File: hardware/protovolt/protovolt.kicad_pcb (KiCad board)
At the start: 2 copper layers, 76 parts, among them J1 Conn_01x03, J10 Conn_02x03_Odd_Even, J2 Conn_01x03, J3 Conn_01x03, J4 Conn_01x03, J5 Conn_01x03, J6 Conn_01x03, J7 Conn_01x03, J8 Conn_01x03, J9 Conn_02x03_Odd_Even, Q1 BSC0702LS, Q2 BSC0702LS, Q3 BSC0702LS, Q4 BSC0702LS, Q5 BSC0702LS, U1 INA226, U2 LM51772RHAR

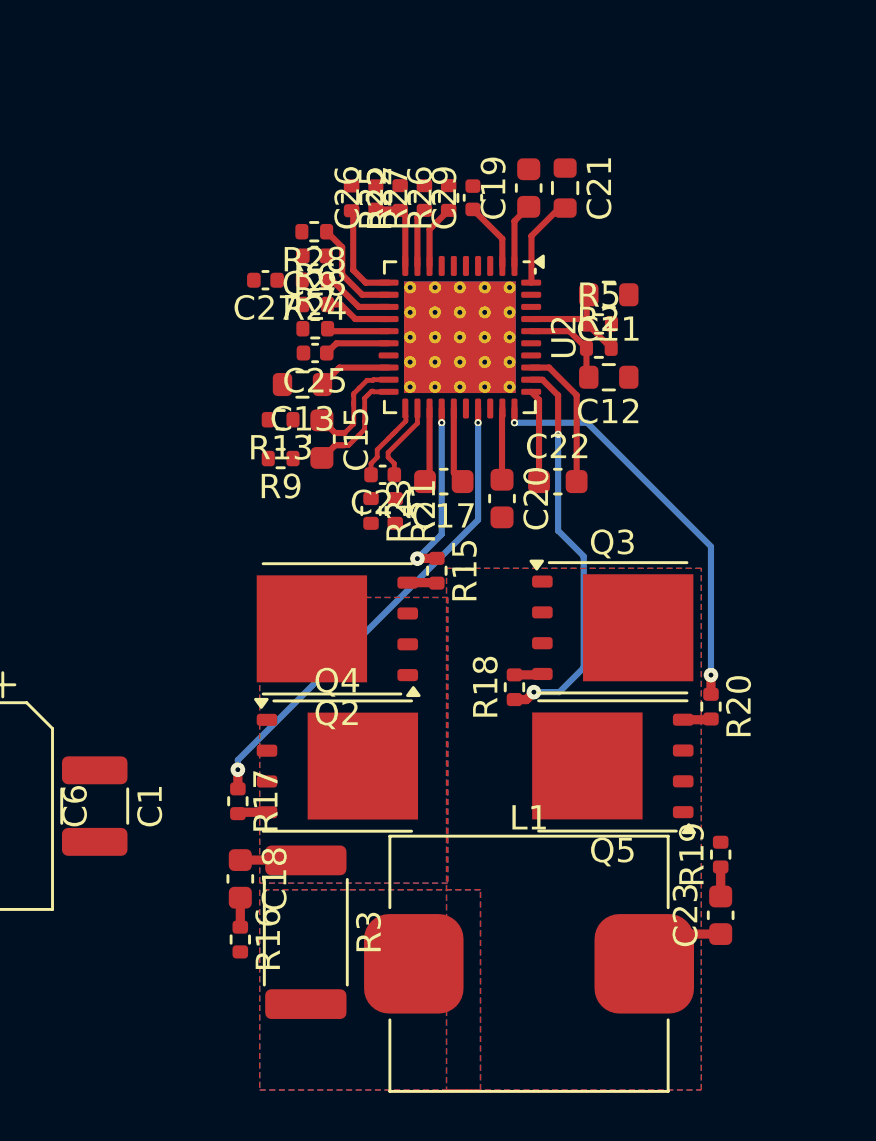
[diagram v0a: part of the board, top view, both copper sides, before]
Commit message: fet routing
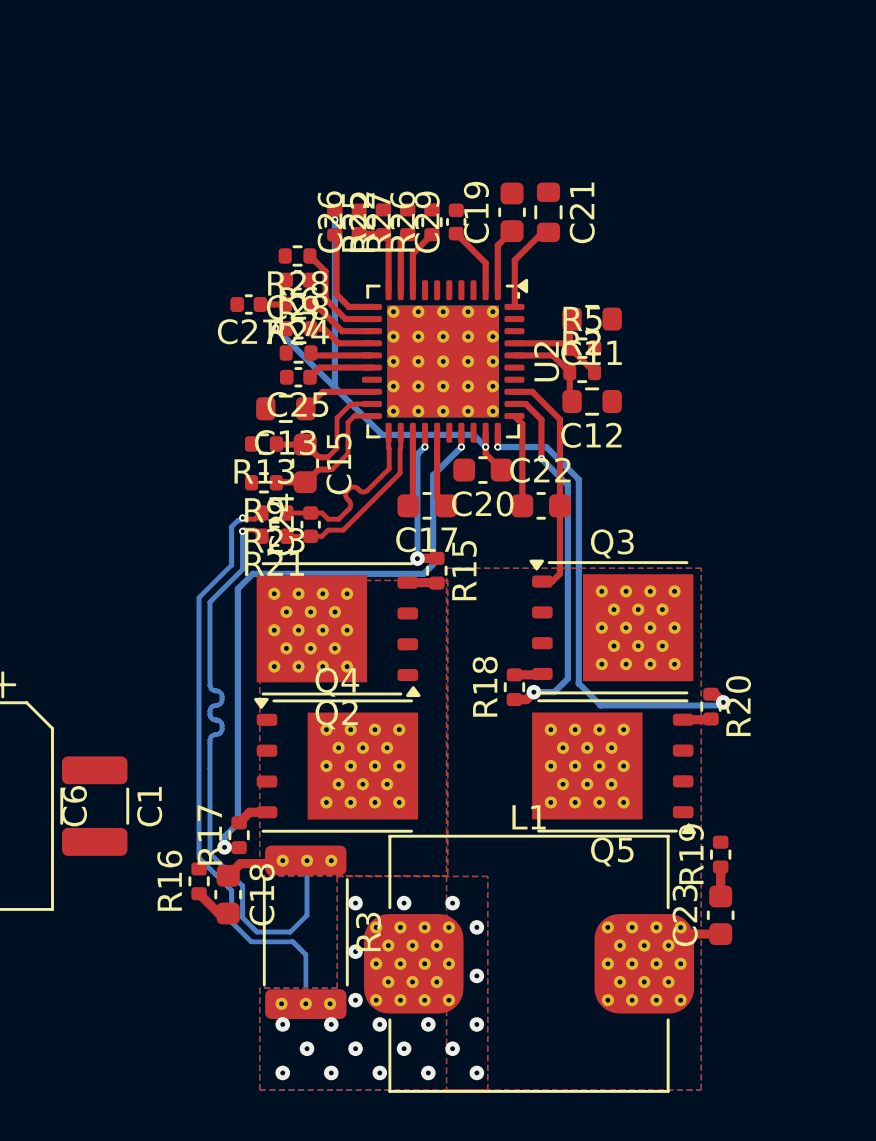
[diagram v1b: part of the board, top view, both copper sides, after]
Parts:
- added ?: , , F.Cu at (179.8, 120.8)
- added ?: , , F.Cu at (172.1, 131.2)
- added ?: , , F.Cu at (171.6, 130.5)
- added ?: , , F.Cu at (181.7, 129.8)
- added ?: , , F.Cu at (166.4, 118.2)
- added ?: , , F.Cu at (166.9, 116.0)
- added ?: , , F.Cu at (169.6, 123.8)
- added ?: , , F.Cu at (181.9, 116.7)
- added ?: , , F.Cu at (166.7, 132.2)
- added ?: , , F.Cu at (179.2, 132.0)
- added ?: , , F.Cu at (168.1, 121.6)
- added ?: , , F.Cu at (166.4, 116.8)
- added ?: , , F.Cu at (178.9, 118.2)
- added ?: , , F.Cu at (176.8, 122.3)
- added ?: , , F.Cu at (166.9, 117.5)
- added ?: , , F.Cu at (170.1, 131.2)
- added ?: , , F.Cu at (165.9, 116.0)
- added ?: , , F.Cu at (169.1, 123.1)
- added ?: , , F.Cu at (171.1, 131.2)
- added ?: , , F.Cu at (169.6, 120.8)
- added ?: , , F.Cu at (165.4, 116.8)
- added ?: , , F.Cu at (178.8, 122.3)
- added ?: , , F.Cu at (167.8, 126.2)
- added ?: , , F.Cu at (171.6, 132.0)
- added ?: , , F.Cu at (168.4, 115.2)
- added ?: , , F.Cu at (178.9, 115.2)
- added ?: , , F.Cu at (179.3, 121.6)
- added ?: , , F.Cu at (170.1, 121.6)
- added ?: , , F.Cu at (168.6, 120.8)
- added ?: , , F.Cu at (180.4, 115.9)
- added ?: , , F.Cu at (182.2, 132.0)
- added ?: , , F.Cu at (166.4, 115.2)
- added ?: , , F.Cu at (171.1, 129.8)
- added ?: , , F.Cu at (170.1, 129.8)
- added ?: , , F.Cu at (170.6, 130.5)
- added ?: , , F.Cu at (179.7, 129.8)
- added ?: , , F.Cu at (181.2, 130.5)
- added ?: , , F.Cu at (171.6, 129.0)
- added ?: , , F.Cu at (179.3, 123.1)
- added ?: , , F.Cu at (167.9, 116.0)
- added ?: , , F.Cu at (181.4, 115.9)
- added ?: , , F.Cu at (180.7, 129.8)
- added ?: , , F.Cu at (170.6, 132.0)
- added ?: , , F.Cu at (180.9, 115.2)
- added ?: , , F.Cu at (180.2, 132.0)
- added ?: , , F.Cu at (177.3, 121.6)
- added ?: , , F.Cu at (179.8, 123.8)
- added ?: , , F.Cu at (170.6, 129.0)
- added ?: , , F.Cu at (178.8, 123.8)
- added ?: , , F.Cu at (177.8, 122.3)
- added ?: , , F.Cu at (179.4, 117.4)
- added ?: , , F.Cu at (167.4, 115.2)
- added ?: , , F.Cu at (177.3, 123.1)
- added ?: , , F.Cu at (177.8, 120.8)
- added ?: , , F.Cu at (172.6, 129.0)
- added ?: , , F.Cu at (165.4, 115.2)
- added ?: , , F.Cu at (178.9, 116.7)
- added ?: , , F.Cu at (172.1, 129.8)
- added ?: , , F.Cu at (169.6, 122.3)
- added ?: , , F.Cu at (179.2, 129.0)
- added ?: , , F.Cu at (169.1, 121.6)
- added ?: , , F.Cu at (180.7, 131.2)
- added ?: , , F.Cu at (167.4, 118.2)
- added ?: , , F.Cu at (181.4, 117.4)
- added ?: , , F.Cu at (167.9, 117.5)
- added ?: , , F.Cu at (167.6, 122.3)
- added ?: , , F.Cu at (176.8, 123.8)
- added ?: , , F.Cu at (166.8, 126.2)
- added ?: , , F.Cu at (165.9, 117.5)
- added ?: , , F.Cu at (168.6, 122.3)
- added ?: , , F.Cu at (172.6, 132.0)
- added ?: , , F.Cu at (182.2, 129.0)
- added ?: , , F.Cu at (181.2, 129.0)
- added ?: , , F.Cu at (176.8, 120.8)
- added ?: , , F.Cu at (181.9, 115.2)
- added ?: , , F.Cu at (177.8, 123.8)
- added ?: , , F.Cu at (168.4, 118.2)
- added ?: , , F.Cu at (181.7, 131.2)
- added ?: , , F.Cu at (179.9, 118.2)
- added ?: , , F.Cu at (169.6, 132.0)
- added ?: , , F.Cu at (168.4, 116.8)
- added ?: , , F.Cu at (165.8, 126.2)
- added ?: , , F.Cu at (172.6, 130.5)
- added ?: , , F.Cu at (167.6, 120.8)
- added ?: , , F.Cu at (178.3, 121.6)
- added ?: , , F.Cu at (180.2, 129.0)
- added ?: , , F.Cu at (165.7, 132.2)
- added ?: , , F.Cu at (181.9, 118.2)
- added ?: , , F.Cu at (179.4, 115.9)
- added ?: , , F.Cu at (169.6, 129.0)
- added ?: , , F.Cu at (179.8, 122.3)
- added ?: , , F.Cu at (167.6, 123.8)
- added ?: , , F.Cu at (170.6, 120.8)
- added ?: , , F.Cu at (167.7, 132.2)
- added ?: , , F.Cu at (178.8, 120.8)
- added ?: , , F.Cu at (167.4, 116.8)
- added ?: , , F.Cu at (179.9, 115.2)
- added ?: , , F.Cu at (169.6, 130.5)
- added ?: , , F.Cu at (170.6, 123.8)
- added ?: , , F.Cu at (179.7, 131.2)
- added ?: , , F.Cu at (180.4, 117.4)
- added ?: , , F.Cu at (168.1, 123.1)
- added ?: , , F.Cu at (180.9, 118.2)
- added ?: , , F.Cu at (180.9, 116.7)
- added ?: , , F.Cu at (168.6, 123.8)
- added ?: , , F.Cu at (181.2, 132.0)
- added ?: , , F.Cu at (179.2, 130.5)
- added ?: , , F.Cu at (180.2, 130.5)
- added ?: , , F.Cu at (179.9, 116.7)
- added ?: , , F.Cu at (178.3, 123.1)
- added ?: , , F.Cu at (165.4, 118.2)
- added ?: , , F.Cu at (170.6, 122.3)
- added ?: , , F.Cu at (170.1, 123.1)
- added ?: , , F.Cu at (182.2, 130.5)
- moved R21 5.08 mm to (165.4, 112.9), turned to 180 degrees
- moved R23 3.98 mm to (165.4, 111.9), turned to 180 degrees
- moved C24 3.61 mm to (166.9, 112.4), turned to 90 degrees
- moved R16 2.94 mm to (162.3, 127.1), turned to 90 degrees
- moved C20 1.41 mm to (174.0, 110.2), turned to 180 degrees
- moved R17 1.40 mm to (163.9, 125.2), turned to 90 degrees
- moved C11 1.21 mm to (178.5, 103.9)
- moved C12 1.21 mm to (178.5, 107.3)
- moved C13 1.21 mm to (165.9, 107.6)
- moved C15 1.21 mm to (166.7, 109.9)
- moved C17 1.21 mm to (171.7, 111.6)
- moved C19 1.21 mm to (175.2, 99.5)
- moved C21 1.21 mm to (176.7, 99.5)
- moved C22 1.21 mm to (176.4, 111.6)
- moved C25 1.21 mm to (166.4, 106.3)
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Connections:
- net /output_A/CSA renamed /output_A/CSR_P
- net /output_A/CSB renamed /output_A/CSR_N
- net /output_A/ISNSN renamed /output_A/ISNSR_N
- net /output_A/ISNSP renamed /output_A/ISNSR_P
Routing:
- net /output_A/CSR_P: track 5.80 -> 32.8 mm, vias 0 -> 1
- net /output_A/CSR_N: track 0.00 -> 24.6 mm, vias 0 -> 22
- net /output_A/VCC2: track 2.94 -> 20.4 mm, vias 0 -> 3
- net Net-(U2-LO1): track 19.8 -> 25.9 mm
- net /output_A/SW2: track 9.77 -> 15.2 mm
- net /output_A/CS_N: track 3.34 -> 7.71 mm
- net /output_A/CS_P: track 3.34 -> 7.42 mm
- net Net-(U2-LO2): track 16.9 -> 19.9 mm
- net Net-(U2-HO2): track 16.4 -> 15.1 mm
- net Net-(U2-HO1): track 7.41 -> 6.13 mm
- net /output_A/ISNS_P: track 4.68 -> 5.88 mm
- net /output_A/ISNS_N: track 4.61 -> 5.81 mm
- net Net-(C27-Pad1): track 0.00 -> 1.04 mm

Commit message: four layer
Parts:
- removed ? (x114): , 
- L1: footprint Inductor_SMD:L_Changjiang_FXL1050 -> protovolt:L_Changjiang_FXL1050
- R3: footprint Resistor_SMD:R_2512_6332Metric -> Resistor_SMD:R_1206_3216Metric
- moved J9 99.0 mm to (235.6, 120.0), turned to -90 degrees
- moved R14 58.0 mm to (204.3, 104.8)
- moved R10 58.0 mm to (204.3, 103.2)
- moved C16 57.7 mm to (202.6, 104.0)
- moved J10 57.4 mm to (140.0, 120.0), turned to 90 degrees
- moved U1 56.5 mm to (198.7, 104.3)
- moved C14 55.8 mm to (200.1, 106.8)
- moved R12 54.1 mm to (196.0, 107.0), turned to 90 degrees
- moved R11 52.9 mm to (196.9, 107.0), turned to 90 degrees
- moved R8 52.1 mm to (197.9, 107.0), turned to 90 degrees
- moved C5 43.1 mm to (227.1, 120.0)
- moved D1 42.7 mm to (215.3, 117.0)
- moved R4 42.6 mm to (212.9, 113.8)
- moved Q1 42.3 mm to (210.6, 117.2)
- moved R1 41.1 mm to (203.0, 118.0)
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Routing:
- net /output_A/ISNSR_N: track 0.00 -> 67.8 mm, vias 0 -> 9
- net /output_A/ISNSR_P: track 3.01 -> 70.2 mm, vias 0 -> 57
- net /output_A/DRV: track 0.00 -> 42.3 mm, vias 0 -> 2
- net /output_A/VCC2: track 20.4 -> 4.44 mm
- net /output_A/CSR_P: track 32.8 -> 23.0 mm, vias 1 -> 18
- net /output_A/SW2: track 15.2 -> 6.38 mm, vias 0 -> 34
- net +3V3: track 0.00 -> 6.73 mm
- net /output_A/CSR_N: track 24.6 -> 19.3 mm, vias 22 -> 32
- net Net-(U2-HO1): track 6.13 -> 11.2 mm
- net Net-(U2-HO2): track 15.1 -> 19.4 mm
- net Net-(U1-Vin-): track 0.00 -> 3.47 mm
- net Net-(D1-K): track 0.00 -> 3.36 mm
- net Net-(J4-Pin_1): track 0.00 -> 3.32 mm
- net Net-(U1-Vin+): track 0.00 -> 2.91 mm
- net Net-(U2-LO2): track 19.9 -> 22.7 mm
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- added copper zone on In1.Cu, net /output_A/CSR_N
- added copper zone on In1.Cu, net /output_A/CSR_P
- added copper zone on B.Cu, net /output_A/ISNSR_N
- added copper zone on F.Cu, net /output_A/ISNSR_N
- added copper zone on In1.Cu, net /output_A/ISNSR_N
- added copper zone on In2.Cu, net /output_A/ISNSR_N
- added copper zone on B.Cu, net /output_A/ISNSR_P
- added copper zone on F.Cu, net /output_A/ISNSR_P
- added copper zone on In1.Cu, net /output_A/ISNSR_P
- added copper zone on In2.Cu, net /output_A/ISNSR_P
- added copper zone on In1.Cu, net /output_A/SW2
- added copper zone on B.Cu, net Net-(D1-A)
- added copper zone on F.Cu, net Net-(D1-A)
- added copper zone on In1.Cu, net Net-(D1-A)
- added copper zone on In2.Cu, net Net-(D1-A)
- added copper zone on B.Cu, net VBUS
- added copper zone on F.Cu, net VBUS
- added copper zone on In1.Cu, net VBUS
- added copper zone on In2.Cu, net VBUS
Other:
- copper layers 2 -> 4

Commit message: wire all
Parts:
- moved J1 139.2 mm to (215.0, 104.0)
- moved J4 123.1 mm to (222.0, 104.0)
- moved J2 102.4 mm to (184.0, 104.0)
- moved J8 98.2 mm to (191.0, 104.0)
- moved J6 71.5 mm to (146.7, 104.0)
- moved J7 70.7 mm to (153.7, 104.0)
- moved J5 61.4 mm to (160.7, 104.0)
- moved J3 57.5 mm to (139.7, 104.0)
- moved C16 2.62 mm to (205.2, 103.5)
- moved R10 2.62 mm to (206.9, 102.8)
- moved R14 2.62 mm to (206.9, 104.3)
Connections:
- J2 pad 3: unconnected-(J2-Pin_3-Pad3) -> GND
- J7 pad 1: /output_A/DTRK -> /output_A/ATRK
- J7 pad 2: /output_A/ATRK -> /output_A/DTRK
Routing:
- net Net-(D1-A): track 0.00 -> 51.9 mm, vias 53 -> 55
- net /output_A/VCC2: track 4.44 -> 53.4 mm, vias 3 -> 5
- net VBUS: track 3.11 -> 41.5 mm, vias 38 -> 40
- net /output_A/MODE: track 0.00 -> 34.1 mm, vias 0 -> 2
- net /output_A/SCL: track 0.00 -> 32.1 mm, vias 0 -> 2
- net Net-(J4-Pin_2): track 1.38 -> 31.3 mm, vias 0 -> 2
- net Net-(J4-Pin_1): track 3.32 -> 31.8 mm, vias 0 -> 2
- net /output_A/SDA: track 0.00 -> 28.3 mm, vias 0 -> 2
- net Net-(J4-Pin_3): track 2.74 -> 27.0 mm, vias 0 -> 2
- net Net-(J1-Pin_2): track 0.00 -> 24.1 mm, vias 0 -> 2
- net /output_A/ATRK: track 2.04 -> 25.4 mm, vias 0 -> 2
- net Net-(J1-Pin_1): track 0.00 -> 21.5 mm, vias 0 -> 2
- net /output_A/DTRK: track 0.00 -> 20.5 mm, vias 0 -> 2
- net /output_A/RST: track 0.55 -> 17.5 mm, vias 1 -> 2
- net /output_A/SYNC: track 0.00 -> 15.7 mm, vias 0 -> 2
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
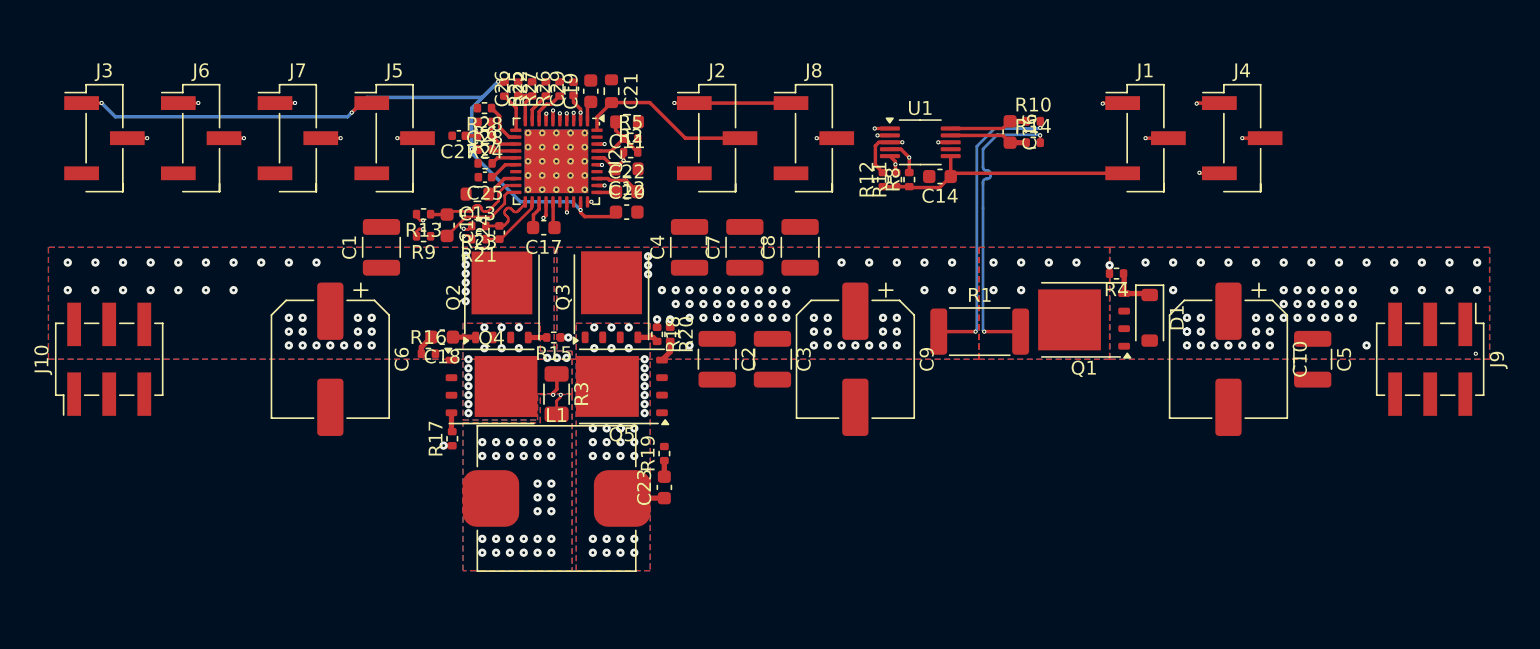
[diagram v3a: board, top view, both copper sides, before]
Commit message: route ground
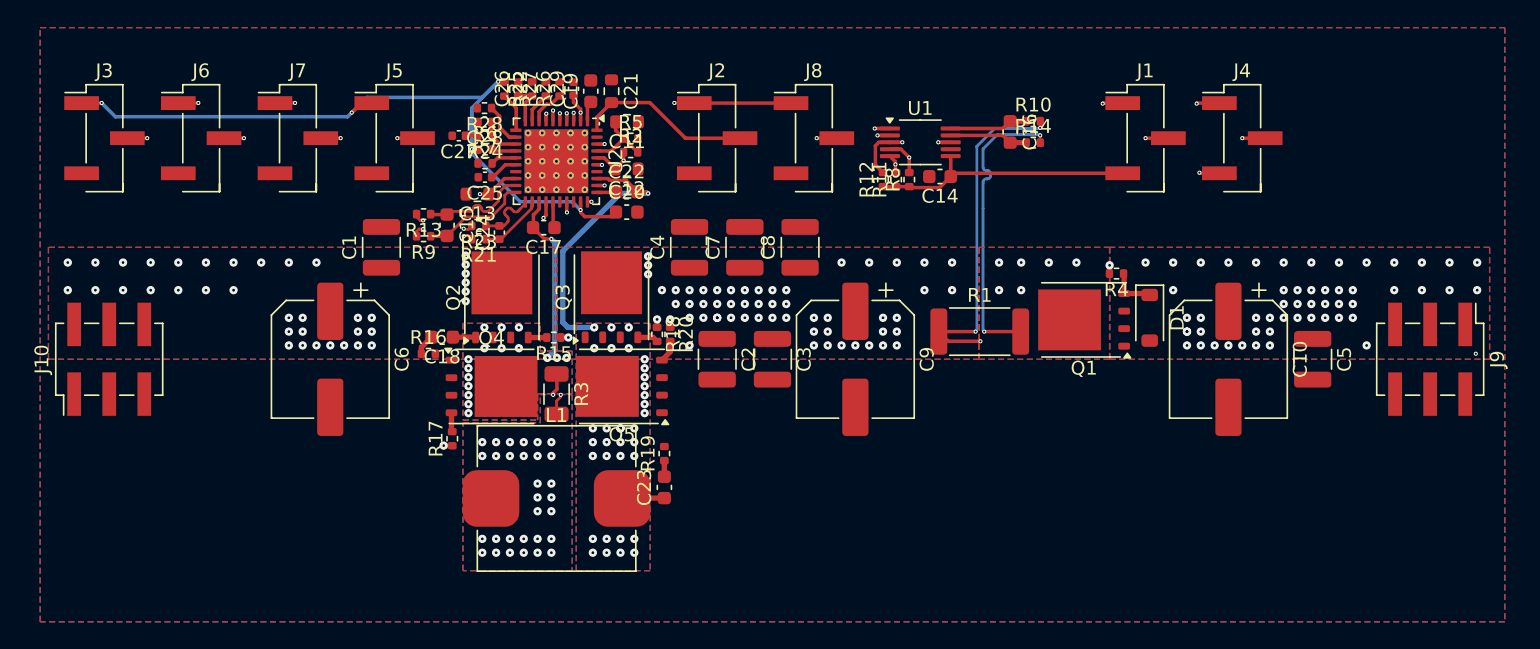
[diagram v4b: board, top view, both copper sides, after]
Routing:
- net /output_A/ISNSR_P: track 73.0 -> 125.0 mm, vias 57 -> 59
- net /output_A/SW2: track 6.38 -> 22.7 mm, vias 34 -> 35
- net /output_A/CSR_P: track 23.0 -> 33.6 mm, vias 18 -> 19
- net /output_A/ISNS_P: track 6.62 -> 7.82 mm
- net /output_A/DRV: track 42.3 -> 41.3 mm
- net VBUS: track 41.5 -> 42.5 mm
- added copper zone on B.Cu, net GND
- added copper zone on F.Cu, net GND
- added copper zone on In1.Cu, net GND
- added copper zone on In2.Cu, net GND

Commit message: finalize DRU & PCB
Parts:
- Q1, Q2, Q3, Q4, Q5: footprint Package_TO_SOT_SMD:TDSON-8-1 -> protovolt:TDSON-8-1
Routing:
- net GND: track 0.00 -> 13.5 mm, vias 0 -> 228
- net /output_A/CSR_P: track 33.6 -> 35.9 mm, vias 19 -> 25
- net /output_A/ISNSR_N: track 70.7 -> 72.8 mm, vias 9 -> 15
- net /output_A/ISNSR_P: track 125.0 -> 127.1 mm, vias 59 -> 69
- net VBUS: track 42.5 -> 44.1 mm, vias 40 -> 57
- net Net-(U2-LO1): track 26.1 -> 27.1 mm
- net Net-(U2-LO2): track 22.7 -> 23.4 mm
- net Net-(U2-HO2): track 19.4 -> 20.0 mm
- net /output_A/CSR_N: track 19.3 -> 19.6 mm, vias 32 -> 38
- net Net-(D1-A): track 51.9 -> 51.8 mm, vias 55 -> 67
- net /output_A/SW2: vias 35 -> 36
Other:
- board outline added: 104.5 x 43 mm
- board text added: "3V3"
- board text added: "50V MAX 36V MAX 1 MHz 2.2 uH"
- board text added: "5V MODE"
- board text added: "5V SYNC"
- board text added: "A0 A1"
- board text added: "ALERT SCL"
- board text added: "ALEX X DAWSON COLLEGE ENRICHED P&E 2025/05/16"
- board text added: "ATRK DTRK"
- board text added: "GND"
- board text added: "LM51772 DEV"
- board text added: "SCL SDA"
- board text added: "SDA"
- board text added: "VBUS BIAS"
- board text added: "VBUS RST"
- board text added: "VIN GND"
- board text added: "VOUT GND"
- board text added: "Vin Vout fsw L1"
